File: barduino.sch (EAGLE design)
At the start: 25 parts, among them Q2 16MHz, X1 MINI-USB-PWR

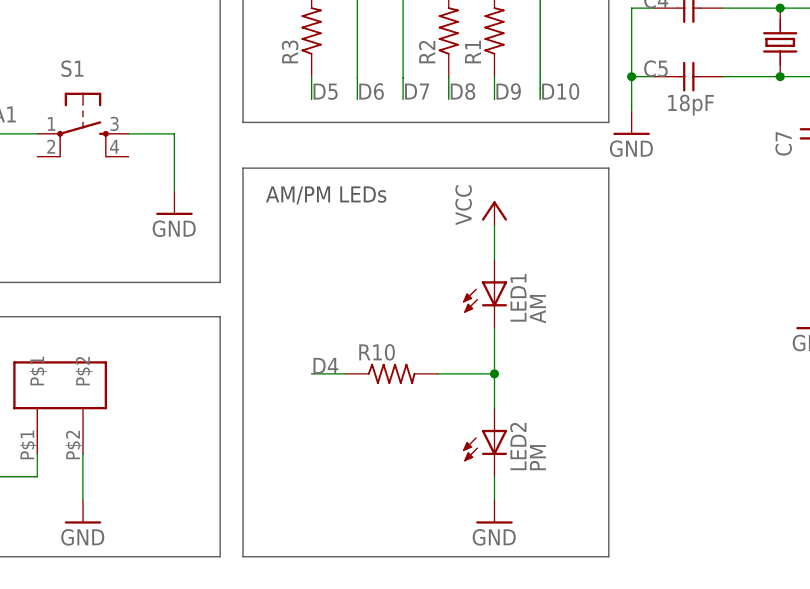
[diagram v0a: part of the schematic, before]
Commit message: update sch to correctly light AM/PM LEDs
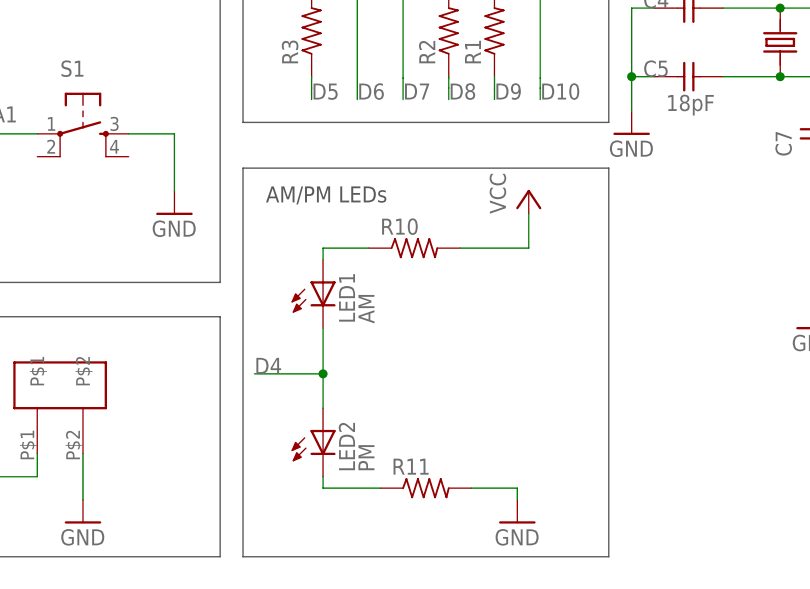
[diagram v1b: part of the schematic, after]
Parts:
- added R11: (no value), resistor:R-US_R1206
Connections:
- removed net N$5: LED1.C, LED2.A, R10.2
- new net N$1: LED1.A, R10.1
- new net N$2: LED2.C, R11.1
- net D4: now also LED1.C, LED2.A; no longer R10.1
- net GND: now also R11.2; no longer LED2.C
- net VCC: now also R10.2; no longer LED1.A
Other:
- moved on the sheet: LED1, LED2, R10
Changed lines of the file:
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@@
 <part name="R8" library="resistor" deviceset="R-US_" device="R1206"/>
 <part name="X1" library="4-Digit-Clock" deviceset="MINI-USB-PWR" device=""/>
+<part name="R11" library="resistor" deviceset="R-US_" device="R1206"/>
 </parts>
 <sheets>
@@
 <instance part="R3" gate="G$1" x="2.54" y="68.58" rot="R90"/>
 <instance part="R4" gate="G$1" x="7.62" y="101.6" rot="R90"/>
-<instance part="LED1" gate="G$1" x="22.86" y="40.64"/>
-<instance part="LED2" gate="G$1" x="22.86" y="24.13"/>
-<instance part="P+5" gate="VCC" x="22.86" y="49.53"/>
-<instance part="GND8" gate="1" x="22.86" y="13.97"/>
-<instance part="R10" gate="G$1" x="11.43" y="30.48"/>
+<instance part="LED1" gate="G$1" x="3.81" y="40.64"/>
+<instance part="LED2" gate="G$1" x="3.81" y="24.13"/>
+<instance part="P+5" gate="VCC" x="26.67" y="50.8"/>
+<instance part="GND8" gate="1" x="25.4" y="13.97"/>
+<instance part="R10" gate="G$1" x="13.97" y="44.45"/>
 <instance part="R5" gate="G$1" x="12.7" y="101.6" rot="R90"/>
 <instance part="R6" gate="G$1" x="17.78" y="101.6" rot="R90"/>
@@
 <instance part="R8" gate="G$1" x="27.94" y="101.6" rot="R90"/>
 <instance part="X1" gate="G$1" x="-30.48" y="99.06" rot="MR0"/>
+<instance part="R11" gate="G$1" x="15.24" y="17.78"/>
 </instances>
 <busses>
@@
 </segment>
 <segment>
-<wire x1="22.86" y1="46.99" x2="22.86" y2="43.18" width="0.1524" layer="91"/>
+<pinref part="R10" gate="G$1" pin="2"/>
+<wire x1="19.05" y1="44.45" x2="26.67" y2="44.45" width="0.1524" layer="91"/>
 <pinref part="P+5" gate="VCC" pin="VCC"/>
-<pinref part="LED1" gate="G$1" pin="A"/>
+<wire x1="26.67" y1="44.45" x2="26.67" y2="48.26" width="0.1524" layer="91"/>
 </segment>
 </net>
@@
 </segment>
 <segment>
+<pinref part="R11" gate="G$1" pin="2"/>
+<wire x1="20.32" y1="17.78" x2="25.4" y2="17.78" width="0.1524" layer="91"/>
 <pinref part="GND8" gate="1" pin="GND"/>
-<wire x1="22.86" y1="16.51" x2="22.86" y2="19.05" width="0.1524" layer="91"/>
-<pinref part="LED2" gate="G$1" pin="C"/>
+<wire x1="25.4" y1="17.78" x2="25.4" y2="16.51" width="0.1524" layer="91"/>
 </segment>
 </net>
@@
 </segment>
 <segment>
-<pinref part="R10" gate="G$1" pin="1"/>
-<wire x1="6.35" y1="30.48" x2="2.54" y2="30.48" width="0.1524" layer="91"/>
-<label x="2.54" y="30.48" size="1.778" layer="95"/>
+<label x="-3.81" y="30.48" size="1.778" layer="95"/>
+<pinref part="LED2" gate="G$1" pin="A"/>
+<wire x1="3.81" y1="26.67" x2="3.81" y2="30.48" width="0.1524" layer="91"/>
+<pinref part="LED1" gate="G$1" pin="C"/>
+<wire x1="3.81" y1="30.48" x2="3.81" y2="35.56" width="0.1524" layer="91"/>
+<junction x="3.81" y="30.48"/>
+<wire x1="-3.81" y1="30.48" x2="3.81" y2="30.48" width="0.1524" layer="91"/>
 </segment>
 </net>
@@
 </segment>
 </net>
-<net name="N$5" class="0">
-<segment>
-<pinref part="LED2" gate="G$1" pin="A"/>
-<wire x1="22.86" y1="26.67" x2="22.86" y2="30.48" width="0.1524" layer="91"/>
-<pinref part="LED1" gate="G$1" pin="C"/>
-<pinref part="R10" gate="G$1" pin="2"/>
-<wire x1="22.86" y1="30.48" x2="22.86" y2="35.56" width="0.1524" layer="91"/>
-<wire x1="16.51" y1="30.48" x2="22.86" y2="30.48" width="0.1524" layer="91"/>
-<junction x="22.86" y="30.48"/>
-</segment>
-</net>
 <net name="N$8" class="0">
 <segment>
@@
 </segment>
 </net>
+<net name="N$1" class="1">
+<segment>
+<pinref part="LED1" gate="G$1" pin="A"/>
+<pinref part="R10" gate="G$1" pin="1"/>
+<wire x1="3.81" y1="44.45" x2="3.81" y2="43.18" width="0.1524" layer="91"/>
+<wire x1="8.89" y1="44.45" x2="3.81" y2="44.45" width="0.1524" layer="91"/>
+</segment>
+</net>
+<net name="N$2" class="0">
+<segment>
+<pinref part="LED2" gate="G$1" pin="C"/>
+<wire x1="3.81" y1="19.05" x2="3.81" y2="17.78" width="0.1524" layer="91"/>
+<pinref part="R11" gate="G$1" pin="1"/>
+<wire x1="3.81" y1="17.78" x2="10.16" y2="17.78" width="0.1524" layer="91"/>
+</segment>
+</net>

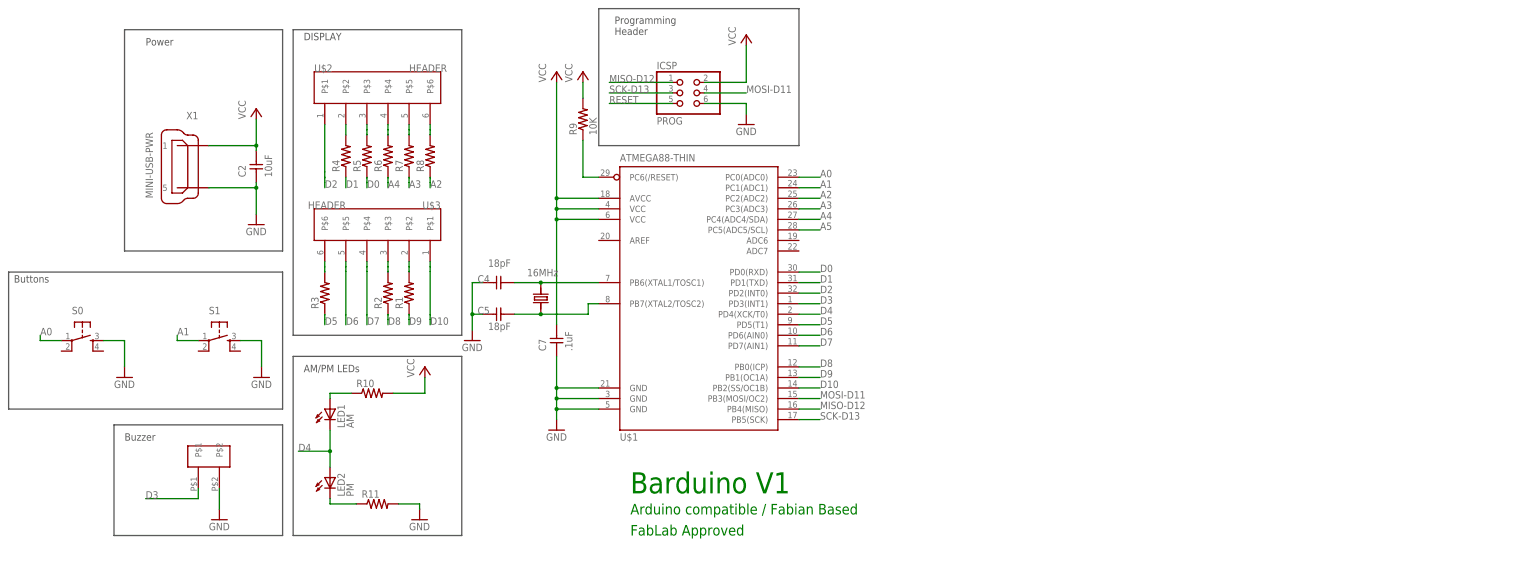
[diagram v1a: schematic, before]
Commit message: align schematic, add another resistor
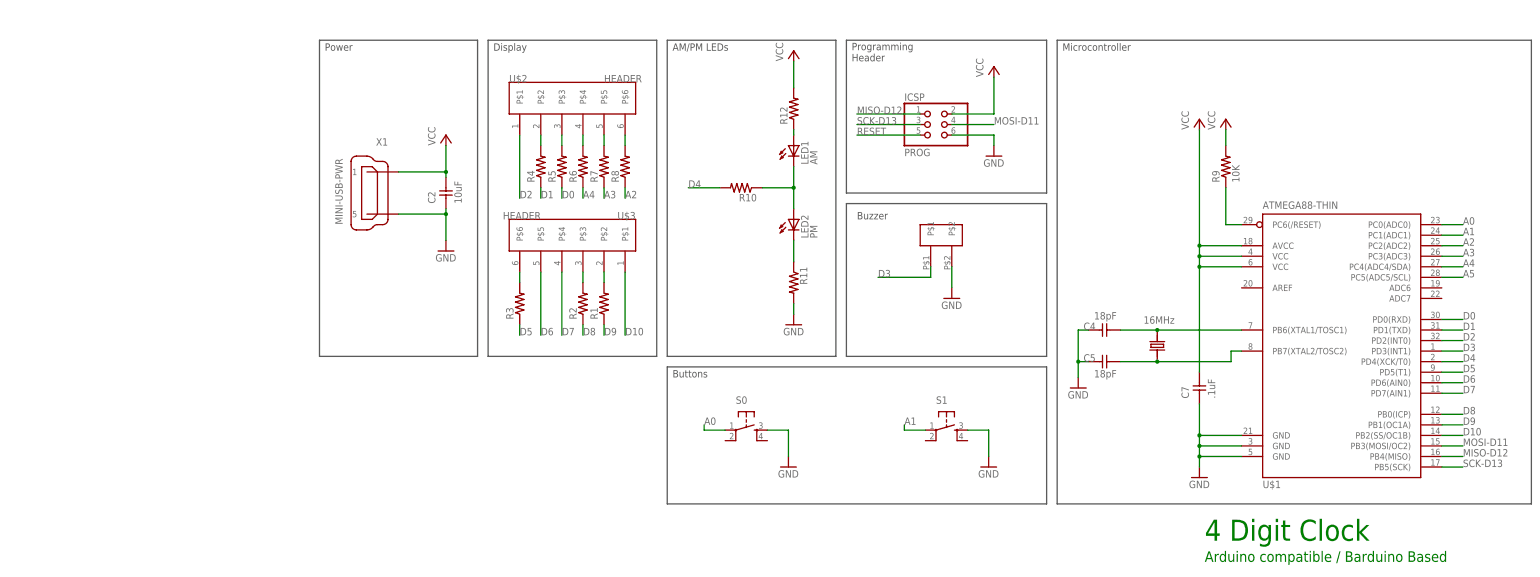
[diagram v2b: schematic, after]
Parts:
- added R12: (no value), resistor:R-US_R1206
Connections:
- net D4: now also R10.1, R10.2
- net N$1: now also R12.1; no longer R10.1
- net VCC: now also R12.2; no longer R10.2
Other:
- note added: "4 Digit Clock"
- note added: "Arduino compatible / Barduino Based"
- note added: "Display"
- note added: "Microcontroller"
- note removed: "Arduino compatible / Fabian Based"
- note removed: "Barduino V1"
- note removed: "DISPLAY"
- note removed: "FabLab Approved"
- moved on the sheet: C2, C4, C5, C7, ICSP, LED1, LED2, R1, R10, R11, R2, R3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

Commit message: fixed mistake on LEDs net
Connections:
- new net N$3: LED1.C, LED2.A, R10.1
- net D4: no longer LED1.C, LED2.A, R10.1
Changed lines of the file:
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@@
-</segment>
-<segment>
-<pinref part="LED2" gate="G$1" pin="A"/>
-<wire x1="115.57" y1="88.9" x2="115.57" y2="93.98" width="0.1524" layer="91"/>
-<pinref part="LED1" gate="G$1" pin="C"/>
-<wire x1="115.57" y1="93.98" x2="115.57" y2="99.06" width="0.1524" layer="91"/>
-<junction x="115.57" y="93.98"/>
-<pinref part="R10" gate="G$1" pin="1"/>
-<wire x1="107.95" y1="93.98" x2="115.57" y2="93.98" width="0.1524" layer="91"/>
 </segment>
 <segment>
@@
 </segment>
 </net>
+<net name="N$3" class="0">
+<segment>
+<pinref part="LED1" gate="G$1" pin="C"/>
+<pinref part="LED2" gate="G$1" pin="A"/>
+<wire x1="115.57" y1="99.06" x2="115.57" y2="93.98" width="0.1524" layer="91"/>
+<pinref part="R10" gate="G$1" pin="1"/>
+<wire x1="115.57" y1="93.98" x2="115.57" y2="88.9" width="0.1524" layer="91"/>
+<wire x1="107.95" y1="93.98" x2="115.57" y2="93.98" width="0.1524" layer="91"/>
+<junction x="115.57" y="93.98"/>
+</segment>
+</net>

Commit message: replace mini usb connector with micro usb
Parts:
- removed X1: MINI-USB-PWR, 4-Digit-Clock:MINI-USB-PWR
- added U$5: MICRO-USB-PWR, 4-Digit-Clock:MICRO-USB-PWR
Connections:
- net GND: now also U$5.5; no longer X1.5
- net VCC: now also U$5.1; no longer X1.1
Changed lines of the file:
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@@
 <?xml version="1.0" encoding="utf-8"?>
 <!DOCTYPE eagle SYSTEM "eagle.dtd">
-<eagle version="8.3.2">
+<eagle version="8.5.1">
 <drawing>
 <settings>
-<setting alwaysvectorfont="yes"/>
+<setting alwaysvectorfont="no"/>
 <setting keepoldvectorfont="yes"/>
 <setting verticaltext="up"/>
@@
 <part name="GND3" library="supply1" library_urn="urn:adsk.eagle:library:371" deviceset="GND" device=""/>
 <part name="U$4" library="4-Digit-Clock" deviceset="BUZZER" device=""/>
-<part name="R1" library="resistor" deviceset="R-US_" device="R1206"/>
-<part name="R2" library="resistor" deviceset="R-US_" device="R1206"/>
-<part name="R3" library="resistor" deviceset="R-US_" device="R1206"/>
-<part name="R4" library="resistor" deviceset="R-US_" device="R1206"/>
-<part name="LED1" library="led" deviceset="LED" device="CHIPLED_1206" value="AM"/>
-<part name="LED2" library="led" deviceset="LED" device="CHIPLED_1206" value="PM"/>
+<part name="R1" library="resistor" library_urn="urn:adsk.eagle:library:348" deviceset="R-US_" device="R1206" package3d_urn="urn:adsk.eagle:package:26062/1"/>
+<part name="R2" library="resistor" library_urn="urn:adsk.eagle:library:348" deviceset="R-US_" device="R1206" package3d_urn="urn:adsk.eagle:package:26062/1"/>
+<part name="R3" library="resistor" library_urn="urn:adsk.eagle:library:348" deviceset="R-US_" device="R1206" package3d_urn="urn:adsk.eagle:package:26062/1"/>
+<part name="R4" library="resistor" library_urn="urn:adsk.eagle:library:348" deviceset="R-US_" device="R1206" package3d_urn="urn:adsk.eagle:package:26062/1"/>
+<part name="LED1" library="led" library_urn="urn:adsk.eagle:library:259" deviceset="LED" device="CHIPLED_1206" package3d_urn="urn:adsk.eagle:package:15823/2" value="AM"/>
+<part name="LED2" library="led" library_urn="urn:adsk.eagle:library:259" deviceset="LED" device="CHIPLED_1206" package3d_urn="urn:adsk.eagle:package:15823/2" value="PM"/>
 <part name="P+5" library="supply1" deviceset="VCC" device=""/>
 <part name="GND8" library="supply1" library_urn="urn:adsk.eagle:library:371" deviceset="GND" device=""/>
-<part name="R12" library="resistor" deviceset="R-US_" device="R1206"/>
-<part name="R5" library="resistor" deviceset="R-US_" device="R1206"/>
-<part name="R6" library="resistor" deviceset="R-US_" device="R1206"/>
-<part name="R7" library="resistor" deviceset="R-US_" device="R1206"/>
-<part name="R8" library="resistor" deviceset="R-US_" device="R1206"/>
-<part name="X1" library="4-Digit-Clock" deviceset="MINI-USB-PWR" device=""/>
-<part name="R11" library="resistor" deviceset="R-US_" device="R1206"/>
-<part name="R10" library="resistor" deviceset="R-US_" device="R1206"/>
+<part name="R12" library="resistor" library_urn="urn:adsk.eagle:library:348" deviceset="R-US_" device="R1206" package3d_urn="urn:adsk.eagle:package:26062/1"/>
+<part name="R5" library="resistor" library_urn="urn:adsk.eagle:library:348" deviceset="R-US_" device="R1206" package3d_urn="urn:adsk.eagle:package:26062/1"/>
+<part name="R6" library="resistor" library_urn="urn:adsk.eagle:library:348" deviceset="R-US_" device="R1206" package3d_urn="urn:adsk.eagle:package:26062/1"/>
+<part name="R7" library="resistor" library_urn="urn:adsk.eagle:library:348" deviceset="R-US_" device="R1206" package3d_urn="urn:adsk.eagle:package:26062/1"/>
+<part name="R8" library="resistor" library_urn="urn:adsk.eagle:library:348" deviceset="R-US_" device="R1206" package3d_urn="urn:adsk.eagle:package:26062/1"/>
+<part name="R11" library="resistor" library_urn="urn:adsk.eagle:library:348" deviceset="R-US_" device="R1206" package3d_urn="urn:adsk.eagle:package:26062/1"/>
+<part name="R10" library="resistor" library_urn="urn:adsk.eagle:library:348" deviceset="R-US_" device="R1206" package3d_urn="urn:adsk.eagle:package:26062/1"/>
+<part name="U$5" library="4-Digit-Clock" deviceset="MICRO-USB-PWR" device=""/>
 </parts>
 <sheets>
@@
 <instance part="R7" gate="G$1" x="69.85" y="99.06" rot="R90"/>
 <instance part="R8" gate="G$1" x="74.93" y="99.06" rot="R90"/>
-<instance part="X1" gate="G$1" x="15.24" y="92.71" rot="MR0"/>
 <instance part="R11" gate="G$1" x="115.57" y="71.12" rot="R270"/>
 <instance part="R10" gate="G$1" x="102.87" y="93.98" rot="R180"/>
+<instance part="U$5" gate="G$1" x="15.24" y="92.71" rot="MR0"/>
 </instances>
 <busses>
@@
 <junction x="31.75" y="97.79"/>
 <wire x1="20.32" y1="97.79" x2="31.75" y2="97.79" width="0.1524" layer="91"/>
-<pinref part="X1" gate="G$1" pin="1"/>
+<pinref part="U$5" gate="G$1" pin="1"/>
 </segment>
 <segment>
@@
 <wire x1="31.75" y1="81.28" x2="31.75" y2="87.63" width="0.1524" layer="91"/>
 <junction x="31.75" y="87.63"/>
-<pinref part="X1" gate="G$1" pin="5"/>
+<pinref part="U$5" gate="G$1" pin="5"/>
 </segment>
 <segment>
@@
 will not be understood (or retained) with this version.
 </note>
+<note version="8.3" severity="warning">
+Since Version 8.3, EAGLE supports the association of 3D packages
+with devices in libraries, schematics, and board files. Those 3D
+packages will not be understood (or retained) with this version.
+</note>
 </compatibility>

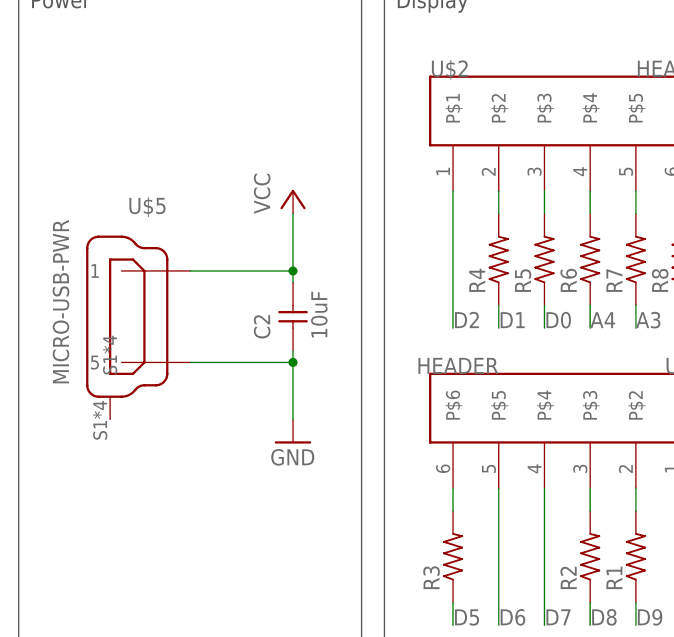
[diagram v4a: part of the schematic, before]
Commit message: connect usb micro connector with jumper
also reduces the board size
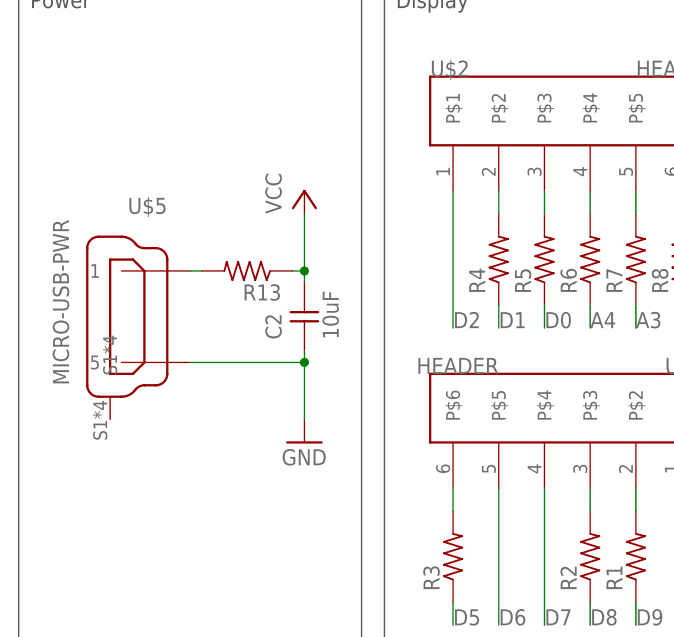
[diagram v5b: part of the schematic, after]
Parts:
- added R13: (no value), resistor:R-US_R1206
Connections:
- net VCC: now also R13.1, R13.2
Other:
- moved on the sheet: C2
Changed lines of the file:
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@@
 <part name="R10" library="resistor" library_urn="urn:adsk.eagle:library:348" deviceset="R-US_" device="R1206" package3d_urn="urn:adsk.eagle:package:26062/1"/>
 <part name="U$5" library="4-Digit-Clock" deviceset="MICRO-USB-PWR" device=""/>
+<part name="R13" library="resistor" library_urn="urn:adsk.eagle:library:348" deviceset="R-US_" device="R1206" package3d_urn="urn:adsk.eagle:package:26062/1"/>
 </parts>
 <sheets>
@@
 </instance>
 <instance part="R9" gate="G$1" x="219.71" y="99.06" rot="R90"/>
-<instance part="P+2" gate="VCC" x="31.75" y="106.68"/>
+<instance part="P+2" gate="VCC" x="33.02" y="106.68"/>
 <instance part="S0" gate="2" x="104.14" y="35.56" rot="R270"/>
-<instance part="C2" gate="1" x="31.75" y="93.98" rot="R90"/>
+<instance part="C2" gate="1" x="33.02" y="93.98" rot="R90"/>
 <instance part="C7" gate="1" x="213.36" y="46.99" rot="R90"/>
 <instance part="U$1" gate="G$1" x="246.38" y="59.69"/>
 <instance part="ICSP" gate="A" x="148.59" y="109.22"/>
 <instance part="GND2" gate="1" x="153.67" y="67.31"/>
-<instance part="GND1" gate="1" x="31.75" y="78.74"/>
+<instance part="GND1" gate="1" x="33.02" y="78.74"/>
 <instance part="P+1" gate="VCC" x="219.71" y="110.49"/>
 <instance part="S1" gate="2" x="152.4" y="35.56" rot="R270"/>
@@
 <instance part="R10" gate="G$1" x="102.87" y="93.98" rot="R180"/>
 <instance part="U$5" gate="G$1" x="15.24" y="92.71" rot="MR0"/>
+<instance part="R13" gate="G$1" x="26.67" y="97.79" rot="R180"/>
 </instances>
 <busses>
@@
 <net name="VCC" class="1">
 <segment>
-<wire x1="31.75" y1="104.14" x2="31.75" y2="97.79" width="0.1524" layer="91"/>
+<wire x1="33.02" y1="104.14" x2="33.02" y2="97.79" width="0.1524" layer="91"/>
 <pinref part="C2" gate="1" pin="2"/>
 <pinref part="P+2" gate="VCC" pin="VCC"/>
-<wire x1="31.75" y1="97.79" x2="31.75" y2="96.52" width="0.1524" layer="91"/>
-<junction x="31.75" y="97.79"/>
-<wire x1="20.32" y1="97.79" x2="31.75" y2="97.79" width="0.1524" layer="91"/>
-<pinref part="U$5" gate="G$1" pin="1"/>
+<wire x1="33.02" y1="97.79" x2="33.02" y2="96.52" width="0.1524" layer="91"/>
+<wire x1="31.75" y1="97.79" x2="33.02" y2="97.79" width="0.1524" layer="91"/>
+<junction x="33.02" y="97.79"/>
+<pinref part="R13" gate="G$1" pin="1"/>
 </segment>
 <segment>
@@
 <wire x1="115.57" y1="118.11" x2="115.57" y2="124.46" width="0.1524" layer="91"/>
 </segment>
+<segment>
+<pinref part="U$5" gate="G$1" pin="1"/>
+<wire x1="21.59" y1="97.79" x2="20.32" y2="97.79" width="0.1524" layer="91"/>
+<pinref part="R13" gate="G$1" pin="2"/>
+</segment>
 </net>
 <net name="GND" class="1">
@@
 <segment>
 <pinref part="C2" gate="1" pin="1"/>
-<wire x1="20.32" y1="87.63" x2="31.75" y2="87.63" width="0.1524" layer="91"/>
-<wire x1="31.75" y1="87.63" x2="31.75" y2="88.9" width="0.1524" layer="91"/>
+<wire x1="20.32" y1="87.63" x2="33.02" y2="87.63" width="0.1524" layer="91"/>
+<wire x1="33.02" y1="87.63" x2="33.02" y2="88.9" width="0.1524" layer="91"/>
 <pinref part="GND1" gate="1" pin="GND"/>
-<wire x1="31.75" y1="81.28" x2="31.75" y2="87.63" width="0.1524" layer="91"/>
-<junction x="31.75" y="87.63"/>
+<wire x1="33.02" y1="81.28" x2="33.02" y2="87.63" width="0.1524" layer="91"/>
+<junction x="33.02" y="87.63"/>
 <pinref part="U$5" gate="G$1" pin="5"/>
 </segment>
